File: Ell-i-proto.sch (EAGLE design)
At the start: 131 parts, among them J1 PROG, J10 EXT-48V, J11 48V, J2 PWMH, J3 PWR, J4 PWML, J5 ANAL, J6 SPI, J7 COMM, J8 ANAH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

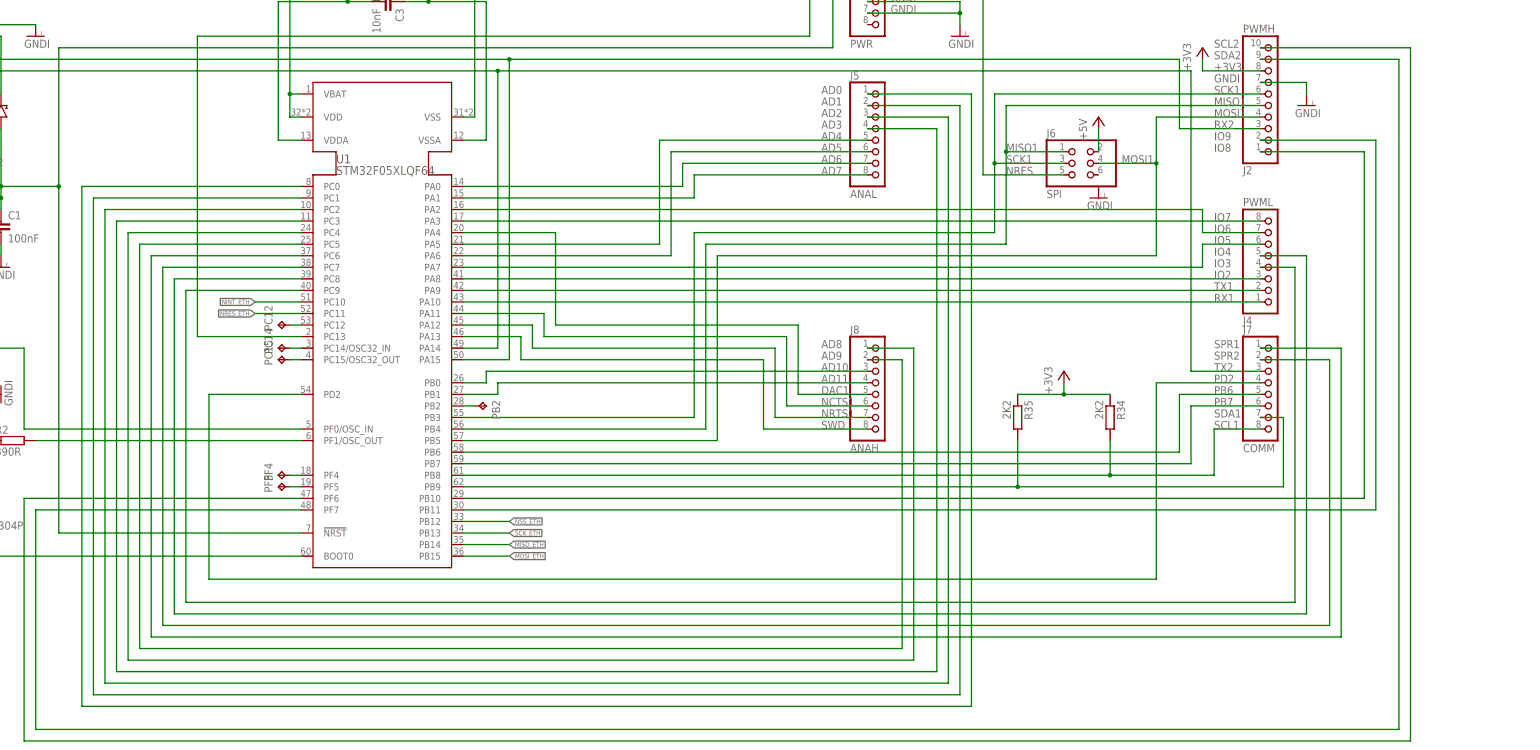
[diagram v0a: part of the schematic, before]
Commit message: Removed more wires.
Fixed missing GNDI in SPI connector.
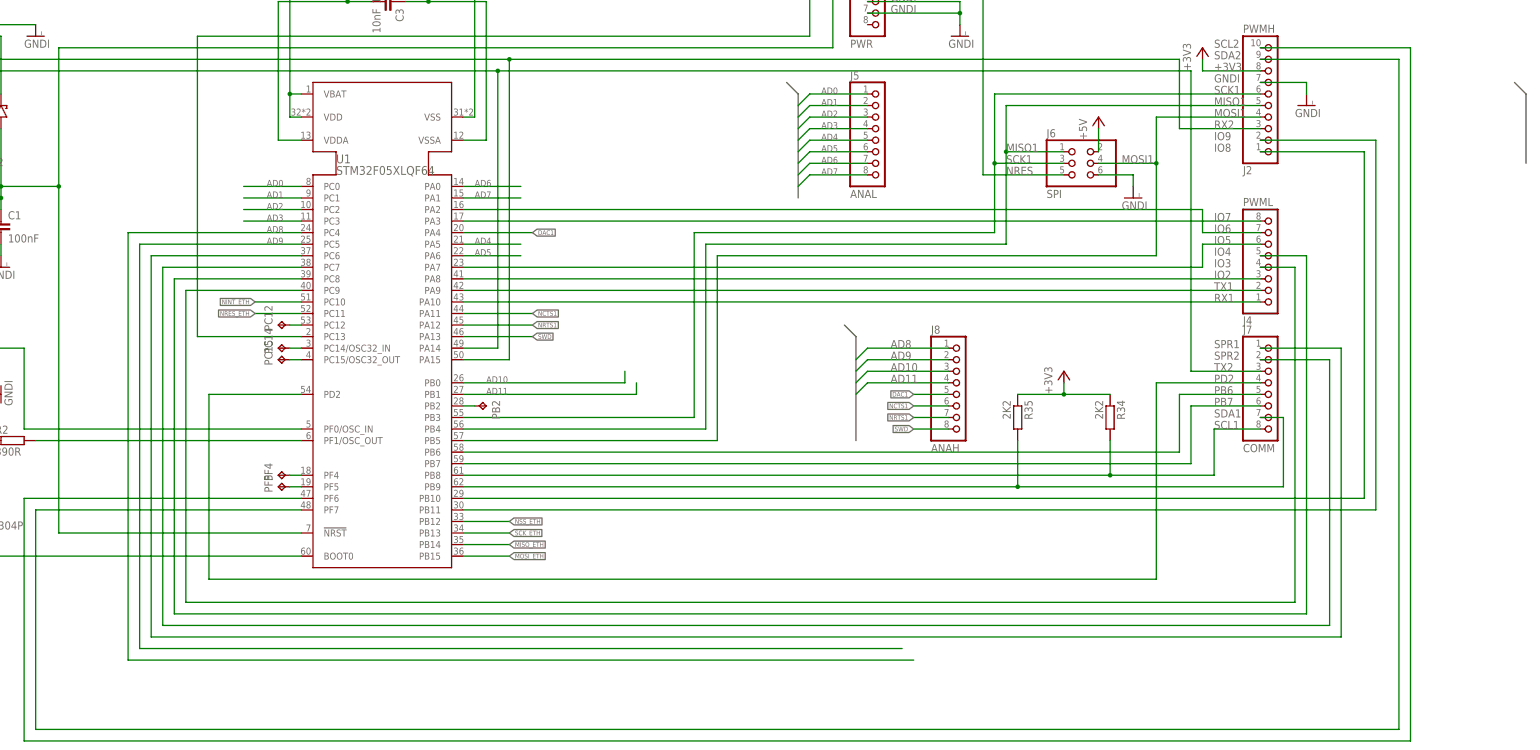
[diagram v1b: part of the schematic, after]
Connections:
- net GNDI: now also J6.6
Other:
- moved on the sheet: J8

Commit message: Removed more wires. Modified schematics layout.
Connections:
- net N205446 renamed PF0
- net N208002 renamed PF1
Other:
- moved on the sheet: C1, C10, C11, C12, C13, C14, C15, C16, C17, C18, C19, C2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

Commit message: Now in three sheets.  Still haven't made Timo's changes to this.
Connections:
- net N06700 renamed MAG-CT-1
- net N06758 renamed MAG-CT-2
- net N07101 renamed RJ45-4-5
- net N08050 renamed RJ45-7-8
- net N35952 renamed RJ45-6
- net N36011 renamed RJ45-1
- net N36095 renamed RJ45-2
- net N64312 renamed RJ45-3
